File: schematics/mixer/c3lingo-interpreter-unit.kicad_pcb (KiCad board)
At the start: 2 copper layers, 229.2 x 90.2 mm, 77 parts, among them J1 Headphone 1, J2 Mic 1, J3 Mix Line-Out, J4 Stage Line-In, J5 PowerSupply, SW1 Mute_1, SW2 OnAir_1, U1 LM833N, U2 NE5534, U3 LM833N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

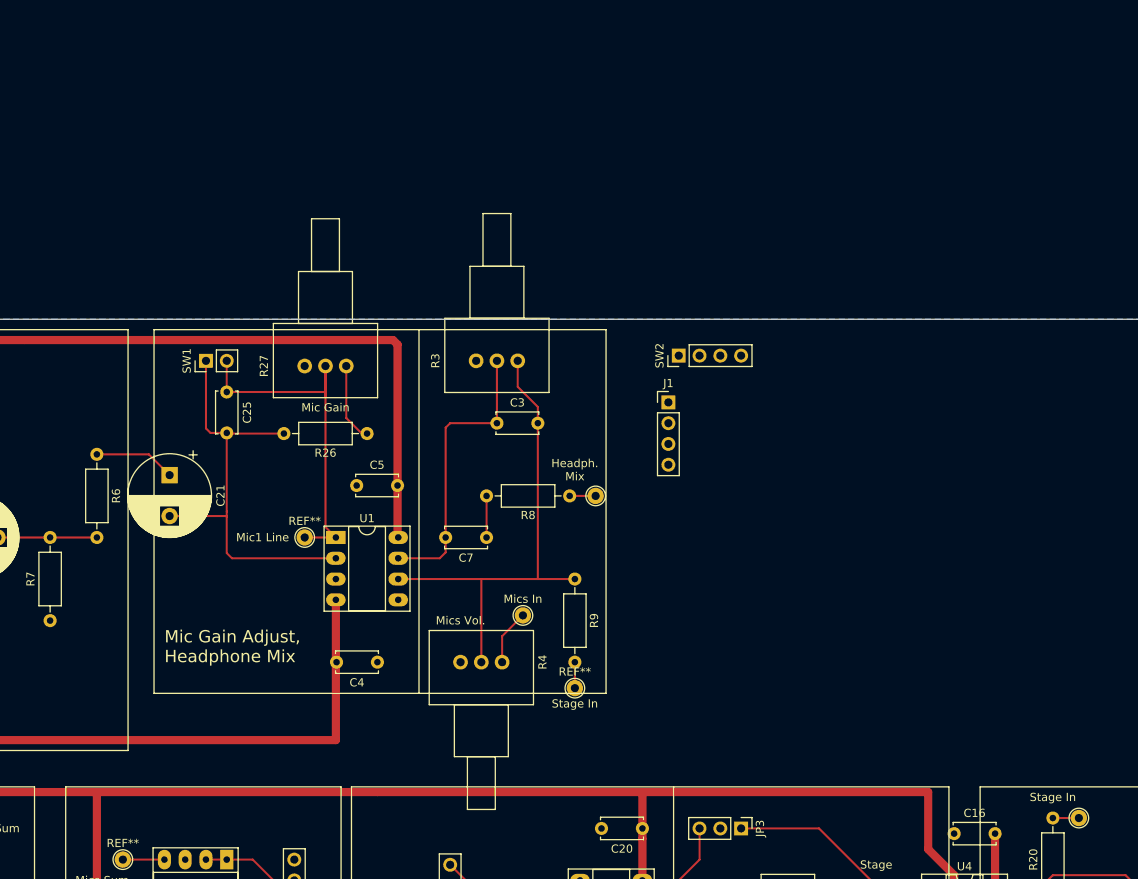
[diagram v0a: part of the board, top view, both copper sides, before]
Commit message: Schematic Main: Add corrected headphone amp
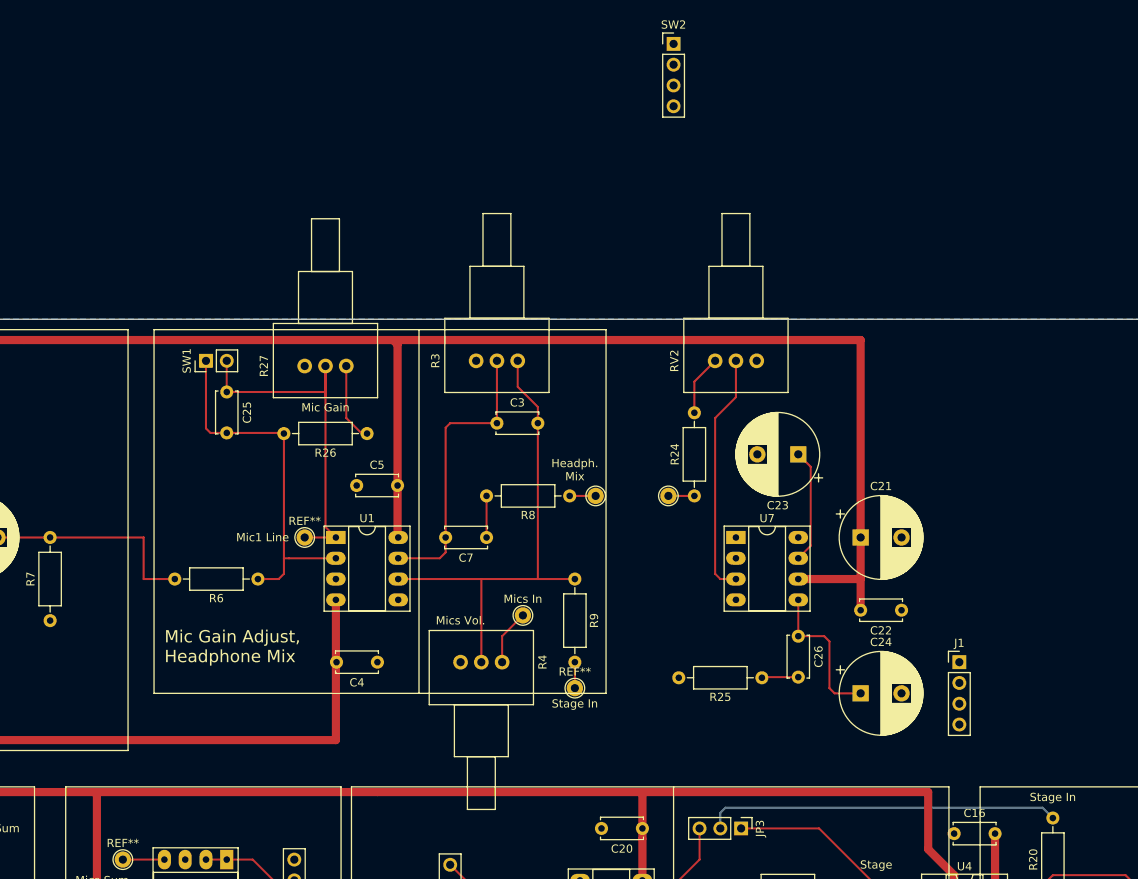
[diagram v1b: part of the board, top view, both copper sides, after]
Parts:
- added C22: 100nF, Capacitor_THT:C_Disc_D5.0mm_W2.5mm_P5.00mm, F.Cu at (198.0, 48.9)
- added C23: 100uF, Capacitor_THT:CP_Radial_D10.0mm_P5.00mm, F.Cu at (185.4, 29.8)
- added C24: 220uF, Capacitor_THT:CP_Radial_D10.0mm_P5.00mm, F.Cu at (193.0, 59.1)
- added C26: 47nF, Capacitor_THT:C_Disc_D5.0mm_W2.5mm_P5.00mm, F.Cu at (185.4, 52.1)
- added R24: R, Resistor_THT:R_Axial_DIN0207_L6.3mm_D2.5mm_P10.16mm_Horizontal, F.Cu at (172.7, 34.9)
- added R25: 12R, Resistor_THT:R_Axial_DIN0207_L6.3mm_D2.5mm_P10.16mm_Horizontal, F.Cu at (181.0, 57.1)
- added RV2: 25K, Potentiometer_THT:Potentiometer_Vishay_148-149_Single_Horizontal, F.Cu at (180.3, 18.4)
- added U7: LM386N-4, Package_DIP:DIP-8_W7.62mm_Socket_LongPads, F.Cu at (177.8, 40.0)
- C21: value 10uF -> 100uF
- R26: value 120R -> 220R
- R6: value 120R -> 820R
- moved C21 84.8 mm to (193.0, 40.0), turned to 0 degrees
- moved REF** 63.8 mm to (169.5, 34.9)
- moved J1 47.7 mm to (205.1, 55.2)
- moved SW2 38.1 mm to (170.2, -20.3), turned to 0 degrees
- moved R6 24.9 mm to (119.4, 45.1), turned to 180 degrees
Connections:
- ? pad 1: (no net) -> Head1
- C21 pad 1: Net-(C21-Pad1) -> +15V
- C21 pad 2: Net-(C21-Pad2) -> GNDREF
- C25 pad 2: Net-(C21-Pad2) -> Net-(C25-Pad2)
- R26 pad 2: Net-(C21-Pad2) -> Net-(C25-Pad2)
- R6 pad 1: Net-(C21-Pad1) -> Net-(C25-Pad2)
- R8 pad 1: (no net) -> Head1
- REF** pad 1: Net-(JP3-Pad2) -> Head1
- SW1 pad 1: Net-(C21-Pad2) -> Net-(C25-Pad2)
- U1 pad 2: Net-(C21-Pad2) -> Net-(C25-Pad2)
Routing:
- net +15V: track 510.9 -> 608.7 mm
- net Net-(C21-Pad2): track 53.4 -> 0.00 mm
- net Net-(C25-Pad2): track 0.00 -> 45.0 mm
- net Net-(JP3-Pad2): track 3.18 -> 43.3 mm
- net Net-(RV2-Pad2): track 0.00 -> 29.9 mm
- net Net-(C24-Pad1): track 0.00 -> 18.3 mm
- net Net-(C6-Pad2): track 12.1 -> 26.8 mm
- net Net-(C23-Pad1): track 0.00 -> 14.0 mm
- net Net-(C21-Pad1): track 9.94 -> 0.00 mm
- net Net-(R24-Pad2): track 0.00 -> 7.40 mm
- net Head1: track 0.00 -> 6.35 mm
- net Net-(C26-Pad2): track 0.00 -> 4.48 mm
- net (no net): track 12.1 -> 8.89 mm

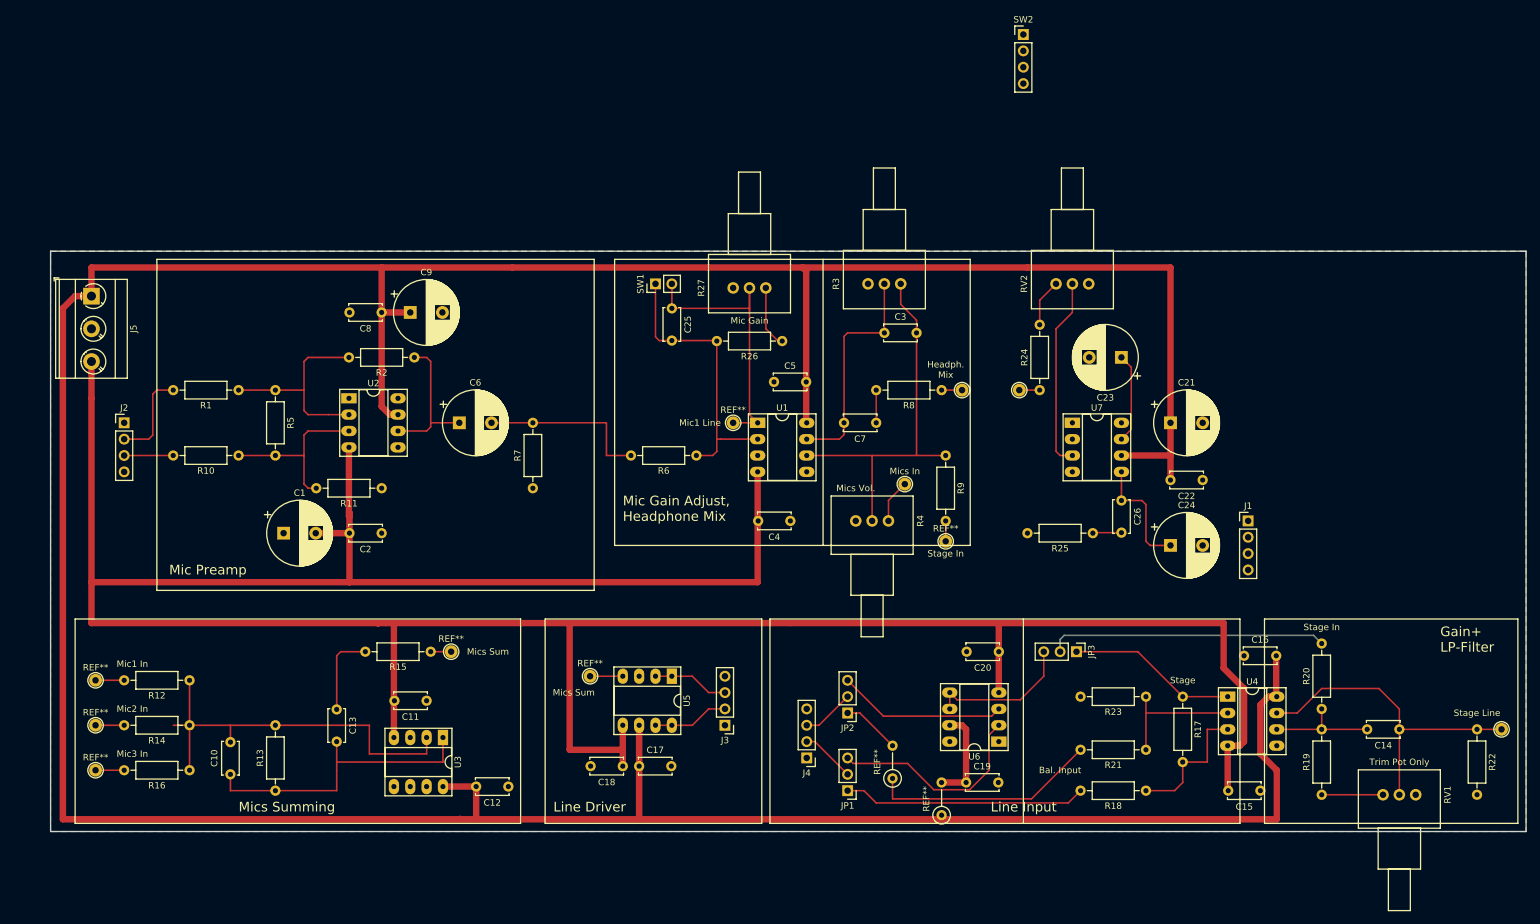
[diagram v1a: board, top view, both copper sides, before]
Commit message: Refine headphone mix requirements, fix signal flow
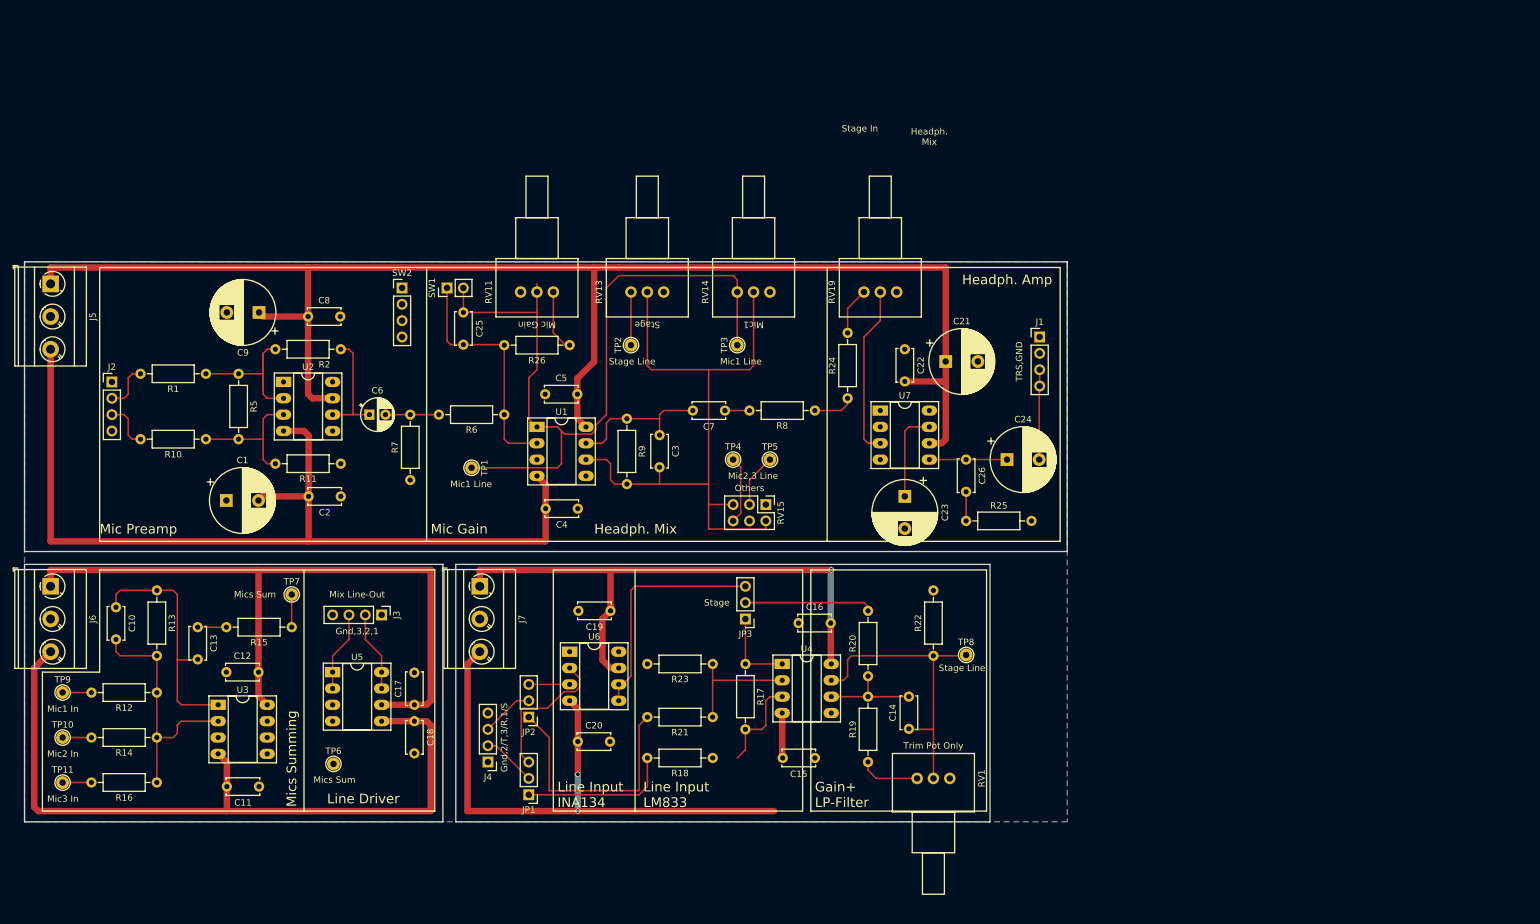
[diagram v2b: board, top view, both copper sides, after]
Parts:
- removed ?, REF** (x6): , TestPoint:TestPoint_THTPad_D2.0mm_Drill1.0mm
- removed Mics In: , TestPoint:TestPoint_THTPad_D2.0mm_Drill1.0mm
- removed REF** (x3): TestPoint_THTPad_D2.0mm_Drill1.0mm, TestPoint:TestPoint_THTPad_D2.0mm_Drill1.0mm
- removed REF** (x2): R_Axial_DIN0207_L6.3mm_D2.5mm_P5.08mm_Vertical, Resistor_THT:R_Axial_DIN0207_L6.3mm_D2.5mm_P5.08mm_Vertical
- added J6: PowerSupply, TerminalBlock_MetzConnect:TerminalBlock_MetzConnect_Type073_RT02603HBLU_1x03_P5.08mm_Horizontal, F.Cu at (19.1, 65.4)
- added J7: PowerSupply, TerminalBlock_MetzConnect:TerminalBlock_MetzConnect_Type073_RT02603HBLU_1x03_P5.08mm_Horizontal, F.Cu at (85.7, 65.4)
- added RV15: 22K, Connector_PinHeader_2.54mm:PinHeader_2x03_P2.54mm_Vertical, F.Cu at (130.2, 52.7)
- added TP1: Mic1, TestPoint:TestPoint_THTPad_D2.0mm_Drill1.0mm, F.Cu at (84.5, 47.0)
- added TP10: Mic2, TestPoint:TestPoint_THTPad_D2.0mm_Drill1.0mm, F.Cu at (20.9, 88.9)
- added TP11: Mic3, TestPoint:TestPoint_THTPad_D2.0mm_Drill1.0mm, F.Cu at (20.9, 95.9)
- added TP2: Stage, TestPoint:TestPoint_THTPad_D2.0mm_Drill1.0mm, F.Cu at (109.2, 27.9)
- added TP3: Mic1, TestPoint:TestPoint_THTPad_D2.0mm_Drill1.0mm, F.Cu at (125.7, 27.9)
- added TP4: Mic2, TestPoint:TestPoint_THTPad_D2.0mm_Drill1.0mm, F.Cu at (125.1, 45.7)
- added TP5: Mic3, TestPoint:TestPoint_THTPad_D2.0mm_Drill1.0mm, F.Cu at (130.8, 45.7)
- added TP6: MicSum, TestPoint:TestPoint_THTPad_D2.0mm_Drill1.0mm, F.Cu at (63.0, 93.0)
- added TP7: MicSum, TestPoint:TestPoint_THTPad_D2.0mm_Drill1.0mm, F.Cu at (56.5, 66.7)
- added TP8: Stage, TestPoint:TestPoint_THTPad_D2.0mm_Drill1.0mm, F.Cu at (161.3, 76.1)
- added TP9: Mic1, TestPoint:TestPoint_THTPad_D2.0mm_Drill1.0mm, F.Cu at (20.9, 81.9)
- C6: footprint Capacitor_THT:CP_Radial_D10.0mm_P5.00mm -> Capacitor_THT:CP_Radial_D5.0mm_P2.50mm
- R24: value R -> 82K
- moved SW2 104.2 mm to (73.7, 19.1)
- moved R22 85.2 mm to (156.2, 76.2), turned to 90 degrees
- moved C14 76.2 mm to (152.4, 87.5), turned to 90 degrees
- moved RV1 72.4 mm to (153.7, 95.2)
- moved R19 70.7 mm to (146.1, 92.7)
- moved R20 70.7 mm to (146.1, 79.4)
- moved C15 69.4 mm to (137.8, 92.1)
- moved C16 69.4 mm to (135.3, 71.1)
- moved U4 69.4 mm to (132.7, 77.5)
- moved R17 68.1 mm to (127.0, 77.5)
- moved U6 68.1 mm to (99.7, 75.6), turned to 0 degrees
- moved R18 67.5 mm to (121.9, 92.1)
- moved R21 67.5 mm to (121.9, 85.7)
- moved R23 67.5 mm to (121.9, 77.5)
- moved C20 66.9 mm to (101.0, 89.5), turned to 0 degrees
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- renumbered R27 to RV11, R3 to RV13, R4 to RV14, RV2 to RV19
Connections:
- J1 pad 1: (no net) -> GNDREF
- J1 pad 2: (no net) -> GNDREF
- R14 pad 2: (no net) -> Net-(R14-Pad2)
- R16 pad 2: (no net) -> Net-(R16-Pad2)
- R9 pad 1: Net-(C3-Pad2) -> Net-(C3-Pad1)
- R9 pad 2: Stage -> Net-(C3-Pad2)
- RV13 pad 1: Net-(C3-Pad2) -> GNDREF
- RV13 pad 2: Net-(C3-Pad1) -> Net-(C3-Pad2)
- RV13 pad 3: (no net) -> Stage
- RV14 pad 3: MicSum -> Mic1
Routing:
- net +15V: track 608.7 -> 436.4 mm, vias 0 -> 1
- net -15V: track 456.7 -> 361.7 mm, vias 0 -> 2
- net Mic1: track 49.4 -> 126.4 mm
- net Net-(C3-Pad2): track 59.4 -> 103.4 mm
- net Net-(C10-Pad2): track 62.9 -> 39.5 mm
- net Net-(JP3-Pad2): track 43.3 -> 19.9 mm
- net Net-(JP2-Pad3): track 26.3 -> 6.35 mm
- net Net-(C6-Pad2): track 26.8 -> 8.30 mm
- net Net-(JP1-Pad1): track 37.8 -> 23.4 mm
- net Net-(JP3-Pad1): track 26.4 -> 12.7 mm
- net Net-(JP3-Pad3): track 22.9 -> 36.3 mm
- net Net-(C3-Pad1): track 35.5 -> 23.1 mm
- net Net-(RV15-Pad6): track 0.00 -> 10.5 mm
- net Net-(JP1-Pad3): track 32.9 -> 22.7 mm
- net MicSum: track 15.0 -> 5.08 mm
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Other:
- board size 229.2 x 90.2 mm -> 162 x 87 mm
- board text added: "Gnd,2/T,3/R,1/S"
- board text added: "Gnd,3,2,1"
- board text added: "Headph. Amp"
- board text added: "Line Input INA134"
- board text added: "Line Input LM833"
- board text added: "Mic1"
- board text added: "Mic2,3 Line"
- board text added: "Mix Line-Out"
- board text added: "Others"
- board text added: "TRS,GND"
- board text removed: "Bal. Input"
- board text removed: "Line Input"
- board text removed: "Mic Gain Adjust, Headphone Mix"
- board text removed: "Mics In"
- board text removed: "Mics Vol."

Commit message: final fixes for first prototype PCB order
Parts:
- added C27: 220p, Capacitor_THT:C_Disc_D5.0mm_W2.5mm_P5.00mm, F.Cu at (120.0, 81.3)
- added R3: 10K, Resistor_THT:R_Axial_DIN0207_L6.3mm_D2.5mm_P10.16mm_Horizontal, F.Cu at (122.6, 91.4)
- added R4: 3.3K, Resistor_THT:R_Axial_DIN0207_L6.3mm_D2.5mm_P10.16mm_Horizontal, F.Cu at (112.4, 95.2)
- C7: value 10nF -> 100nF
- R17, R18, R21, R23: value R -> 10K
- R24: value 82K -> 820K
- R8: value 47R -> 10K
- moved R8 59.1 mm to (112.4, 91.4), turned to 90 degrees
- moved R18 24.8 mm to (122.6, 67.3), turned to 270 degrees
- moved C7 20.8 mm to (144.0, 43.2)
- moved R21 20.7 mm to (112.4, 67.3), turned to 270 degrees
- moved R23 8.64 mm to (128.9, 82.5), turned to 270 degrees
- moved R17 7.85 mm to (128.9, 69.8)
- moved JP3 6.99 mm to (134.0, 70.5)
- moved C15 3.18 mm to (141.0, 92.1)
- moved C16 3.18 mm to (138.4, 71.1)
- moved RV1 3.18 mm to (156.8, 95.2)
- moved TP8 3.18 mm to (164.5, 76.1)
- moved C14 3.17 mm to (155.6, 87.5)
- moved R19 3.17 mm to (149.2, 92.7)
- moved R20 3.17 mm to (149.2, 79.4)
- moved R22 3.17 mm to (159.4, 76.2)
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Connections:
- C7 pad 2: Net-(C3-Pad1) -> Net-(C7-Pad2)
- J1 pad 1: GNDREF -> (no net)
- J1 pad 2: GNDREF -> (no net)
- R18 pad 2: Net-(JP1-Pad1) -> Net-(C27-Pad1)
- R21 pad 2: Net-(JP2-Pad1) -> Net-(C27-Pad2)
- R24 pad 1: Head1 -> Net-(C3-Pad1)
- R8 pad 1: Head1 -> Net-(JP2-Pad1)
- R8 pad 2: Net-(C7-Pad1) -> Net-(C27-Pad2)
- RV19 pad 2: Net-(RV19-Pad2) -> Net-(C7-Pad2)
- U4 pad 2: Net-(R21-Pad1) -> Net-(R17-Pad2)
- U4 pad 3: Net-(R17-Pad2) -> Net-(R21-Pad1)
- U7 pad 3: Net-(RV19-Pad2) -> Net-(C7-Pad1)
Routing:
- net Net-(C7-Pad2): track 0.00 -> 30.9 mm
- net Net-(RV19-Pad2): track 26.7 -> 0.00 mm
- net MicSum: track 5.08 -> 31.6 mm
- net Net-(C3-Pad1): track 23.1 -> 46.5 mm
- net Net-(R21-Pad1): track 19.0 -> 37.2 mm
- net -15V: track 361.7 -> 374.5 mm
- net Net-(JP1-Pad1): track 23.4 -> 35.2 mm
- net Net-(R17-Pad2): track 15.0 -> 25.3 mm
- net Net-(JP3-Pad3): track 36.3 -> 43.3 mm
- net Net-(C27-Pad2): track 0.00 -> 6.43 mm
- net Head1: track 6.41 -> 0.00 mm
- net Net-(C27-Pad1): track 0.00 -> 6.35 mm
- net Net-(JP2-Pad1): track 38.7 -> 34.0 mm
- net Net-(JP3-Pad2): track 19.9 -> 16.1 mm
- net +15V: track 436.4 -> 439.5 mm
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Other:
- outline, holes or cut-outs redrawn
- net class Default: clearance 0.2 -> 0.25
- net class Power: clearance 0.2 -> 0.3
- rule trace_clearance: 0.2 -> 0.25
- board text added: "c3lingo Interpreter Unit v0.1 2020-11-12 Jannik Beyerstedt"
- board text removed: "Stage In"
- board text removed: "c3lingo Interpreter Unit v0.1 Prototyping Modules Jannik Beyerstedt"
